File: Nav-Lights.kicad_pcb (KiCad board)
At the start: 4 copper layers, 50.5 x 52.5 mm, 30 parts, among them U1 LMC555xCMX, U2 LT8374RUFM-WPBF, U3 TPS7B8133QDGNRQ1

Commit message: Touching up layout
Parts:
- added 3V3: 3V3, _NavLights:HARWIN_S1751-46R, F.Cu at (152.0, 107.1)
- added G***: LOGO, LOGO, F.Cu at (115.0, 94.5)
- added GND: TP_GND, _NavLights:HARWIN_S1751-46R, F.Cu at (139.2, 107.1)
- added ISN : TP_ISN, _NavLights:HARWIN_S1751-46R, F.Cu at (132.2, 107.1)
- added SIGNAL: TP_SIGNAL, _NavLights:HARWIN_S1751-46R, F.Cu at (145.6, 107.1)
- added TP2: TP_THR, _NavLights:HARWIN_S1751-46R, F.Cu at (160.0, 125.0)
- added VIN_DRV: MountingHole_Pad, MountingHole:MountingHole_6mm_Pad_TopBottom, F.Cu at (176.0, 95.5)
- added VIN_RTN: MountingHole_Pad, MountingHole:MountingHole_6mm_Pad_TopBottom, F.Cu at (176.0, 110.0)
- H1, H4: footprint MountingHole:MountingHole_3.2mm_M3_DIN965_Pad -> MountingHole:MountingHole_3.2mm_M3_Pad
- H2: renamed from H3; footprint MountingHole:MountingHole_3.2mm_M3_DIN965_Pad -> MountingHole:MountingHole_3.2mm_M3_Pad
- H3: renamed from H2; footprint MountingHole:MountingHole_3.2mm_M3_DIN965_Pad -> MountingHole:MountingHole_3.2mm_M3_Pad
- moved H3 16.2 mm to (175.0, 66.0)
- moved H1 16.0 mm to (116.0, 66.0)
- moved H4 9.22 mm to (175.0, 125.0)
- moved H2 8.73 mm to (116.0, 125.0)
- moved D1 7.80 mm to (126.1, 104.2)
- moved D2 7.80 mm to (126.1, 99.5)
- moved D3 7.80 mm to (126.1, 94.8)
- moved D4 7.80 mm to (126.1, 90.2)
- moved D5 7.80 mm to (126.1, 85.5)
- renumbered C10 to C1, C12 to C10, C8 to C11, C9 to C12, C11 to C5, C5 to C6, C6 to C7, C7 to C8, C1 to C9, R3 to R1, R1 to R3, R5 to R4, R4 to R5, U3 to U2, U2 to U3
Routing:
- net +3V3: track 23.6 -> 30.0 mm
- net /Main/THR: track 10.9 -> 17.0 mm
- net GND: track 11.1 -> 9.17 mm, vias 19 -> 20
- net /Main/ISN: track 3.87 -> 5.67 mm
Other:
- board size 50.5 x 52.5 mm -> 75 x 75 mm
- board text added: "NavLights Dev"
- board text added: "Nolan KM"

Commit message: Adding in HV stuff
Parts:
- removed the G*** at (115.0, 94.5)
- added G***: LOGO, LOGO, F.Cu at (135.0, 120.5)
- added G***: LOGO, LOGO, F.Cu at (176.0, 84.5)

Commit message: name change
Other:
- board text added: "NolanKaz"
- board text removed: "Nolan KM"
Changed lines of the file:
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@@
 		(layer "Edge.Cuts")
 	)
-	(gr_text "Nolan KM"
+	(gr_text "NolanKaz"
 		(at 125 123 0)
 		(layer "F.SilkS")

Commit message: Finishing up layout
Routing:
- net /Main/ISN: track 5.67 -> 3.87 mm
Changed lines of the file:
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@@
 		(at 158 89 90)
 		(property "Reference" "C12"
-			(at 0.2 6 180)
+			(at 0 0 180)
 			(layer "F.SilkS")
 			(effects
@@
 		(start 156.85 100.608871)
 		(end 156.85 105.041171)
-		(width 0.2)
+		(width 0.4)
 		(layer "F.Cu")
 		(net 2)
@@
 		(start 158.799958 106.691213)
 		(end 158.799958 105.041171)
-		(width 0.3)
+		(width 0.4)
 		(layer "F.Cu")
 		(net 4)
@@
 		(start 157.9 107.1)
 		(end 152 107.1)
-		(width 0.3)
+		(width 0.4)
 		(layer "F.Cu")
 		(net 4)
@@
 		(start 160.325 109.116171)
 		(end 160.325 114.905)
-		(width 0.3)
+		(width 0.4)
 		(layer "F.Cu")
 		(net 4)
@@
 		(start 158.35 107.141171)
 		(end 160.325 109.116171)
-		(width 0.3)
+		(width 0.4)
 		(layer "F.Cu")
 		(net 4)
@@
 	)
 	(segment
-		(start 132.2 107.1)
-		(end 132.2 105.3)
-		(width 0.3)
-		(layer "F.Cu")
-		(net 9)
-	)
-	(segment
 		(start 141.5 96.1)
 		(end 141.6 96)
@@
 		(polygon
 			(pts
-				(xy 125.8 105.5) (xy 136.6 105.5) (xy 142.2 97.4) (xy 142.2 96.2) (xy 140.8 96.2) (xy 140.8 97.4)
-				(xy 135.4 105) (xy 125.8 105)
+				(xy 125 106.3) (xy 136.046913 106.3) (xy 142.2 97.4) (xy 142.2 96.2) (xy 140.8 96.2) (xy 140.8 97.4)
+				(xy 135.4 105) (xy 125 105)
 			)
 		)
@@
 		(polygon
 			(pts
-				(xy 170 103.5) (xy 183 103.5) (xy 183 87.5) (xy 169.5 87.5) (xy 169.5 89) (xy 167.5 91) (xy 163 91)
-				(xy 163 92) (xy 160 95) (xy 156 95) (xy 153.5 92.5) (xy 153.5 97) (xy 149.5 97) (xy 149.5 99.7)
-				(xy 157.5 99.7) (xy 157.5 97.5) (xy 161.5 97.5) (xy 161.5 99.7) (xy 167.2 99.7) (xy 170 102.5)
-			)
-		)
+				(xy 170 103) (xy 183 103) (xy 183 87.6) (xy 163 87.6) (xy 163 92) (xy 160 95) (xy 156 95) (xy 153.5 92.5)
+				(xy 153.5 97) (xy 149.5 97) (xy 149.5 99.7) (xy 157.5 99.7) (xy 157.5 97.5) (xy 161.5 97.5) (xy 161.5 99.7)
+				(xy 168.2 99.7) (xy 170 101.5)
+			)
+		)

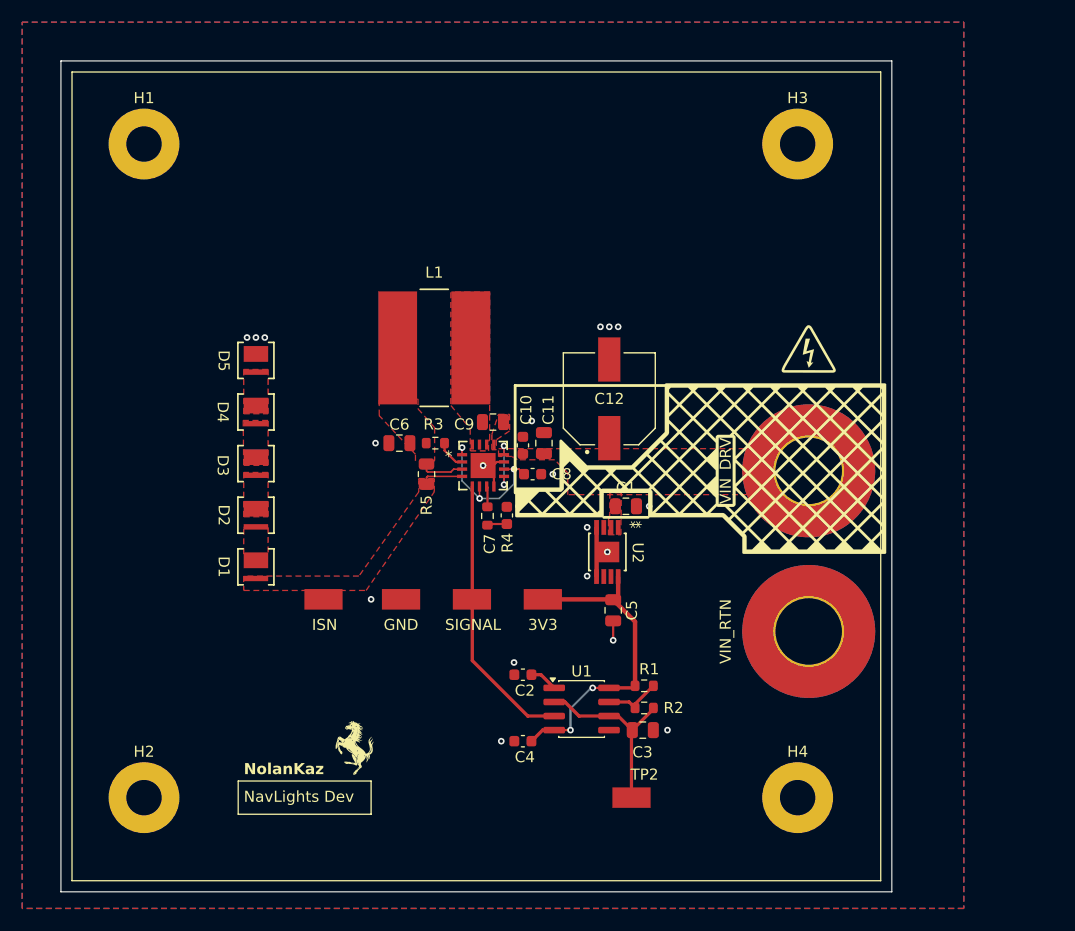
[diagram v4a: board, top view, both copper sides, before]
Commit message: starting cirular pcb
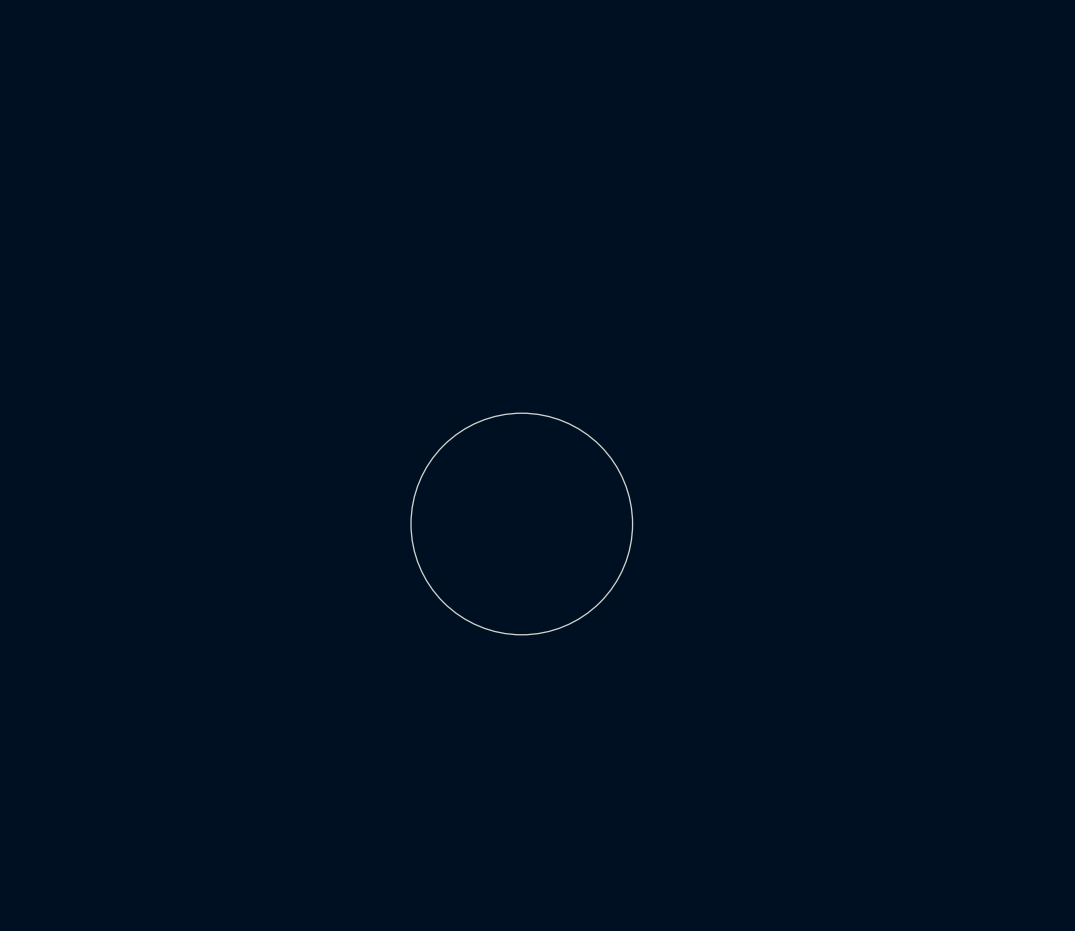
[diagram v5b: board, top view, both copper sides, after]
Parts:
- removed 3V3: 3V3, _NavLights:HARWIN_S1751-46R
- removed C1, C11, C5: 10uF, Capacitor_SMD:C_0805_2012Metric
- removed C10: 1uF, Capacitor_SMD:C_0603_1608Metric
- removed C12: 47uF, _NavLights:CAP_EEEFN2A100L
- removed C2, C4: 0.1uF, Capacitor_SMD:C_0603_1608Metric
- removed C3: 0.27, Capacitor_SMD:C_0805_2012Metric
- removed C6: 4.7uF, Capacitor_SMD:C_0805_2012Metric
- removed C7: 47pF, Capacitor_SMD:C_0603_1608Metric
- removed C8: 2.2uF, Capacitor_SMD:C_0603_1608Metric
- removed C9: 22nf, Capacitor_SMD:C_0805_2012Metric
- removed D1, D2, D3, D4, D5: LED, _NavLights:LED_JB3030AWT_3X3_CRE
- removed G*** (x2): LOGO, LOGO
- removed GND: TP_GND, _NavLights:HARWIN_S1751-46R
- removed H1, H2, H3, H4: MountingHole, MountingHole:MountingHole_3.2mm_M3_Pad
- removed ISN : TP_ISN, _NavLights:HARWIN_S1751-46R
- removed L1: 150uH, _NavLights:IND_BOURNS_SRN1060
- removed R1: 100kOHm, Resistor_SMD:R_0603_1608Metric
- removed R2: 2490kOHm, Resistor_SMD:R_0603_1608Metric
- removed R3: 274kOhm, Resistor_SMD:R_0603_1608Metric
- removed R4: 10kO, Resistor_SMD:R_0603_1608Metric
- removed R5: 24mO, Resistor_SMD:R_0805_2012Metric
- removed SIGNAL: TP_SIGNAL, _NavLights:HARWIN_S1751-46R
- removed TP2: TP_THR, _NavLights:HARWIN_S1751-46R
- removed U1: LMC555xCMX, Package_SO:SOIC-8_3.9x4.9mm_P1.27mm
- removed U2: TPS7B8133QDGNRQ1, _NavLights:VSSOP8_DGN_TEX
- removed U3: LT8374RUFM-WPBF, _NavLights:05-08-1799_ADI
- removed VIN_DRV, VIN_RTN: MountingHole_Pad, MountingHole:MountingHole_6mm_Pad_TopBottom
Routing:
- net +3V3: track 30.0 -> 0.00 mm, vias 2 -> 0
- net /Main/signal: track 25.2 -> 0.00 mm
- net /Main/THR: track 17.0 -> 0.00 mm
- net /Main/INTVCC: track 14.0 -> 0.00 mm, vias 3 -> 0
- net GND: track 9.17 -> 0.00 mm, vias 20 -> 0
- net Net-(U1-DIS): track 5.26 -> 0.00 mm
- net /Main/VIN: track 5.05 -> 0.00 mm, vias 2 -> 0
- net /Main/ISP: track 3.97 -> 0.00 mm
- net /Main/ISN: track 3.87 -> 0.00 mm
- net Net-(U3-FB): track 2.69 -> 0.00 mm
- net Net-(U1-GND): track 2.54 -> 0.00 mm
- net Net-(U3-VC): track 1.86 -> 0.00 mm
- net Net-(C7-Pad1): track 1.79 -> 0.00 mm
- removed copper zone on F.Cu, net /Main/ISN
- removed copper zone on F.Cu, net /Main/ISP
- removed copper zone on F.Cu, net /Main/VIN
- removed copper zone on B.Cu, net GND
- removed copper zone on F.Cu, net GND
- removed copper zone on F.Cu, net Net-(C9-Pad2)
- removed copper zone on F.Cu, net Net-(D1-K)
- removed copper zone on F.Cu, net Net-(D2-K)
- removed copper zone on F.Cu, net Net-(D3-K)
- removed copper zone on F.Cu, net Net-(D4-K)
- removed copper zone on F.Cu, net Net-(U3-BST)
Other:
- board size 75 x 75 mm -> 20 x 20 mm
- board text removed: "NavLights Dev"
- board text removed: "NolanKaz"

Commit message: optlayout
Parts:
- added C1: 10uF, Capacitor_SMD:C_0805_2012Metric, F.Cu at (145.0, 79.6)
- added C10: 1uF, Capacitor_SMD:C_0603_1608Metric, B.Cu at (178.2, 125.0)
- added C11: 10uF, Capacitor_SMD:C_0805_2012Metric, B.Cu at (176.4, 124.8)
- added C12: 47uF, _NavLights:CAP_EEEFN2A100L, B.Cu at (170.8, 127.7)
- added C3: 0.27, Capacitor_SMD:C_0805_2012Metric, F.Cu at (145.0, 82.6)
- added C4: 0.1uF, Capacitor_SMD:C_0603_1608Metric, F.Cu at (140.8, 79.3)
- added C5: 10uF, Capacitor_SMD:C_0805_2012Metric, F.Cu at (145.0, 85.6)
- added C6: 4.7uF, Capacitor_SMD:C_0805_2012Metric, B.Cu at (189.3, 127.3)
- added C7: 47pF, Capacitor_SMD:C_0603_1608Metric, B.Cu at (177.6, 130.1)
- added C8: 2.2uF, Capacitor_SMD:C_0603_1608Metric, B.Cu at (177.4, 127.3)
- added C9: 22nf, Capacitor_SMD:C_0805_2012Metric, B.Cu at (182.5, 122.9)
- added D1: LED, _NavLights:LED_0606 (M1616), F.Cu at (180.2, 87.0)
- added D2: LED, _NavLights:LED_0606 (M1616), F.Cu at (182.9, 87.0)
- added D3: LED, _NavLights:LED_0606 (M1616), F.Cu at (180.2, 89.8)
- added D4: LED, _NavLights:LED_0606 (M1616), F.Cu at (182.8, 89.8)
- added L1: 22uH, _NavLights:IND_AMDLA4020S-220MT, B.Cu at (187.3, 124.1)
- added R1: 100kOHm, Resistor_SMD:R_0603_1608Metric, F.Cu at (140.8, 89.4)
- added R2: 2490kOHm, Resistor_SMD:R_0603_1608Metric, F.Cu at (140.8, 91.9)
- added R3: 274kOhm, Resistor_SMD:R_0603_1608Metric, B.Cu at (186.0, 127.3)
- added R4: 10kO, Resistor_SMD:R_0603_1608Metric, B.Cu at (180.6, 130.1)
- added R5: 24mO, Resistor_SMD:R_0805_2012Metric, B.Cu at (186.6, 129.4)
- added U1: LMC555CMMX, Package_SO:SOIC-8_3.9x4.9mm_P1.27mm, B.Cu at (165.8, 114.5)
- added U2: TPS7B8133QWDRVRQ1, _NavLights:SON65P200X200X80-7N, B.Cu at (196.5, 116.1)
- added U3: LT8374RUFM-WPBF, _NavLights:05-08-1799_ADI, B.Cu at (181.7, 126.6)
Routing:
- net /Main/ISP: track 0.00 -> 5.75 mm
- net /Main/ISN: track 0.00 -> 4.67 mm
- net Net-(U3-FB): track 0.00 -> 2.03 mm
- net /Main/INTVCC: track 0.00 -> 1.78 mm
- net Net-(U3-VC): track 0.00 -> 1.62 mm
- net Net-(C7-Pad1): track 0.00 -> 1.40 mm
- added copper zone on B.Cu, net /Main/ISP
- added copper zone on B.Cu, net GND
- added copper zone on F.Cu, net GND
- added copper zone on B.Cu, net Net-(C9-Pad2)
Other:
- board size 20 x 20 mm -> 35 x 10 mm

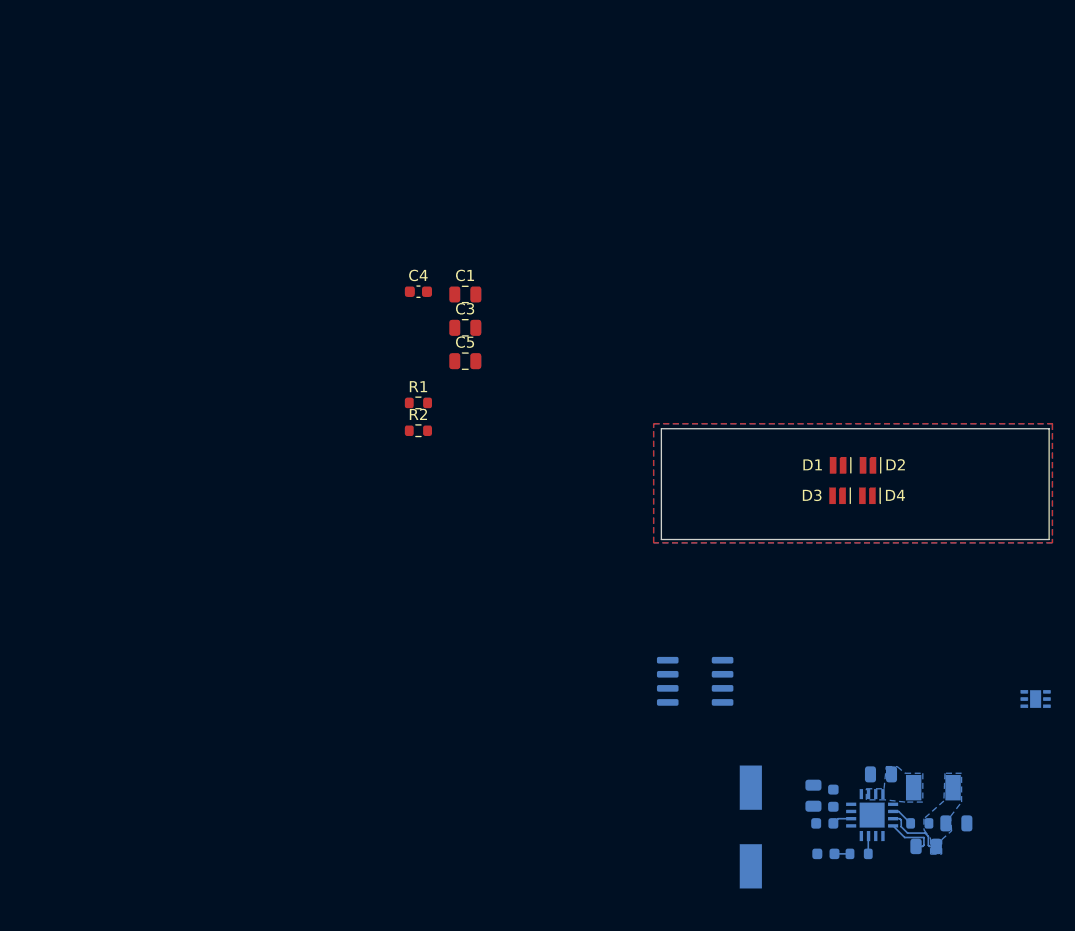
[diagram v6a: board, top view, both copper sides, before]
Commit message: new opt layout
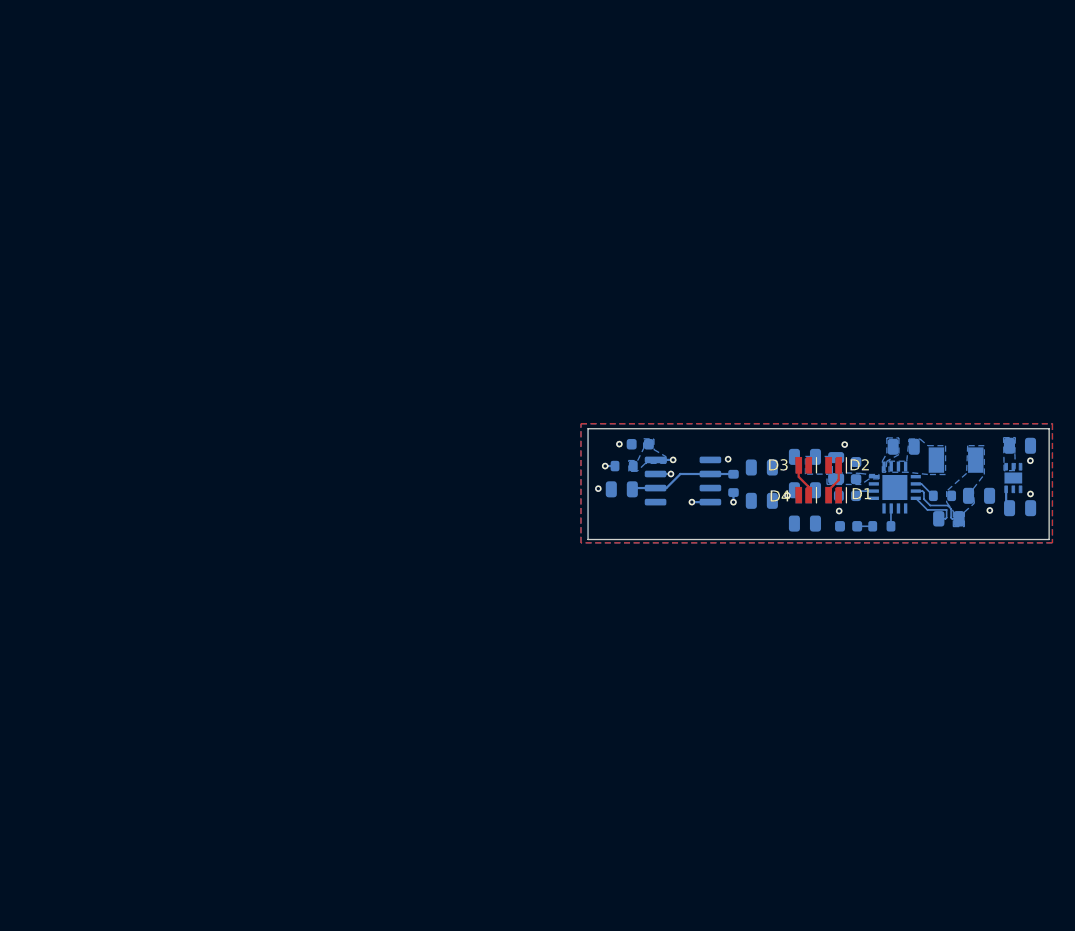
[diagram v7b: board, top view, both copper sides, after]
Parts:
- added C13: 10uF, Capacitor_SMD:C_0805_2012Metric, B.Cu at (175.7, 97.2)
- added C14: 10uF, Capacitor_SMD:C_0805_2012Metric, B.Cu at (175.7, 100.3)
- added C15: 10uF, Capacitor_SMD:C_0805_2012Metric, B.Cu at (171.8, 95.2)
- added C16: 10uF, Capacitor_SMD:C_0805_2012Metric, B.Cu at (171.8, 98.2)
- C1, C4, C5, R1, R2: moved to B.Cu
- C12: value 47uF -> 10uF; footprint _NavLights:CAP_EEEFN2A100L -> Capacitor_SMD:C_0805_2012Metric
- C3: value 0.27 -> 0.27uF; moved to B.Cu
- moved C1 51.9 mm to (195.1, 93.2)
- moved C5 51.8 mm to (195.1, 98.9)
- moved C12 33.8 mm to (175.7, 94.2), turned to 180 degrees
- moved C11 29.6 mm to (178.5, 95.3)
- moved C6 29.6 mm to (191.4, 97.8)
- moved C8 29.6 mm to (179.5, 97.8)
- moved C9 29.6 mm to (184.6, 93.3)
- moved R3 29.6 mm to (188.1, 97.8)
- moved R5 29.6 mm to (188.7, 99.8)
- moved U3 29.6 mm to (183.8, 97.0)
- moved C10 29.6 mm to (180.3, 95.5)
- moved C7 29.6 mm to (179.6, 100.5)
- moved L1 29.6 mm to (189.3, 94.5)
- moved R4 29.6 mm to (182.6, 100.5)
- moved R2 28.8 mm to (169.2, 96.6), turned to 90 degrees
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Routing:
- net /Main/THR: track 0.00 -> 9.71 mm
- net +3V3: track 0.00 -> 5.31 mm, vias 0 -> 2
- net Net-(U1-DIS): track 0.00 -> 3.14 mm, vias 0 -> 3
- net Net-(D3-K): track 0.00 -> 3.07 mm
- net Net-(D1-K): track 0.00 -> 3.07 mm
- net GND: vias 0 -> 1
- net (no net): vias 0 -> 8
- added copper zone on B.Cu, net +3V3
- added copper zone on B.Cu, net /Main/VIN
- added copper zone on B.Cu, net Net-(D2-K)
- added copper zone on B.Cu, net Net-(U3-BST)
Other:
- board size 35 x 10 mm -> 41.6 x 10 mm

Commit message: Layout w/ connector
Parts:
- added J1: Conn_01x02_Pin, Connector_AMASS:AMASS_XT30U-M_1x02_P5.0mm_Vertical, F.Cu at (130.9, 96.2)
- C4, C7: footprint Capacitor_SMD:C_0603_1608Metric -> Capacitor_SMD:C_0402_1005Metric
- C9: footprint Capacitor_SMD:C_0805_2012Metric -> Capacitor_SMD:C_0402_1005Metric
- R1, R2, R3, R4: footprint Resistor_SMD:R_0603_1608Metric -> Resistor_SMD:R_0402_1005Metric
- moved C5 65.5 mm to (130.0, 91.4), turned to 180 degrees
- moved U2 61.1 mm to (133.5, 91.7), turned to 180 degrees
- moved C1 58.2 mm to (136.9, 91.4)
- moved C13 35.7 mm to (140.3, 92.6), turned to 90 degrees
- moved C14 35.5 mm to (140.4, 96.3), turned to -90 degrees
- moved C6 34.9 mm to (156.5, 95.4)
- moved C9 34.9 mm to (149.8, 91.3)
- moved R3 34.4 mm to (153.8, 94.9)
- moved R5 34.1 mm to (154.6, 97.4)
- moved C11 33.8 mm to (144.8, 92.5)
- moved U3 33.8 mm to (150.1, 94.5)
- moved L1 33.8 mm to (155.6, 92.1)
- moved C10 33.8 mm to (146.6, 92.7)
- moved R4 33.5 mm to (149.2, 97.8)
- moved C12 33.2 mm to (142.5, 92.6), turned to 90 degrees
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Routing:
- net GND: track 0.00 -> 69.6 mm, vias 1 -> 17
- net /Main/INTVCC: track 1.78 -> 23.8 mm, vias 0 -> 3
- net /Main/VIN: track 0.00 -> 11.4 mm, vias 0 -> 2
- net +3V3: track 5.31 -> 13.3 mm
- net Net-(U1-DIS): track 3.14 -> 0.00 mm, vias 3 -> 0
- net Net-(D3-K): track 3.07 -> 6.19 mm
- net /Main/ISN: track 4.67 -> 7.52 mm, vias 0 -> 1
- net Net-(U3-BST): track 0.00 -> 1.41 mm
- net /Main/ISP: track 5.75 -> 5.16 mm
- net (no net): vias 8 -> 0
- added copper zone on F.Cu, net Net-(D2-K)
- added copper zone on B.Cu, net Net-(U1-DIS)
- removed copper zone on B.Cu, net +3V3
- removed copper zone on B.Cu, net Net-(U3-BST)
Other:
- board size 41.6 x 10 mm -> 40 x 10 mm
